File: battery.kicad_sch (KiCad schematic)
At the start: 41 parts, among them J1 Lipo, Q1 2N7002, Q2 IRLZ44N, Q3 AO3401A, Q4 IRLZ44N, SW1 SW_Push, SW2 SW_SPST, U1 BQ76920PW

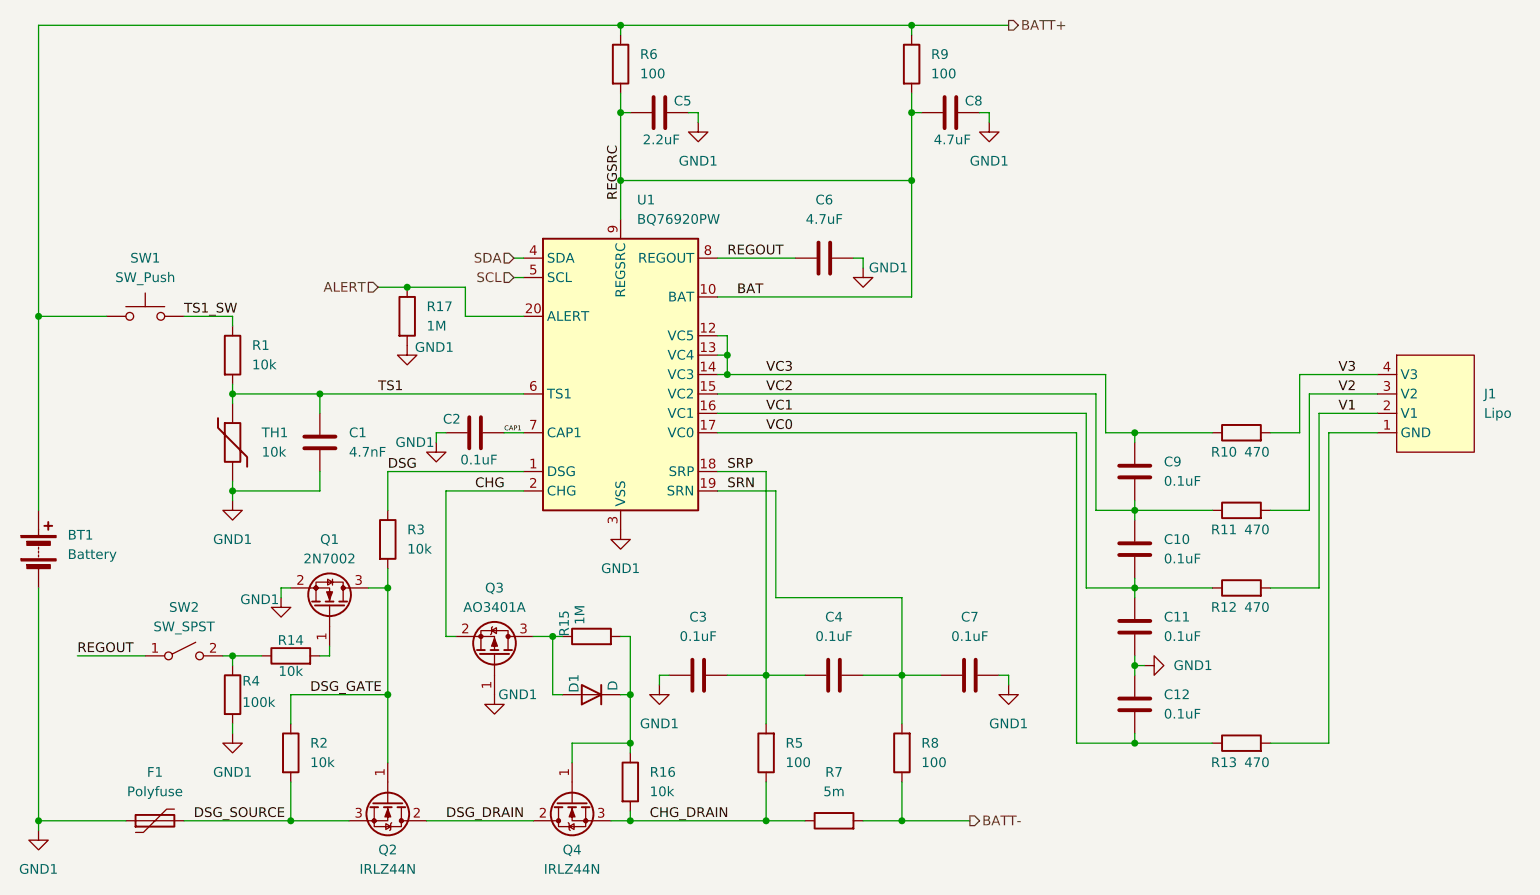
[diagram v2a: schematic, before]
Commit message: add frontleds
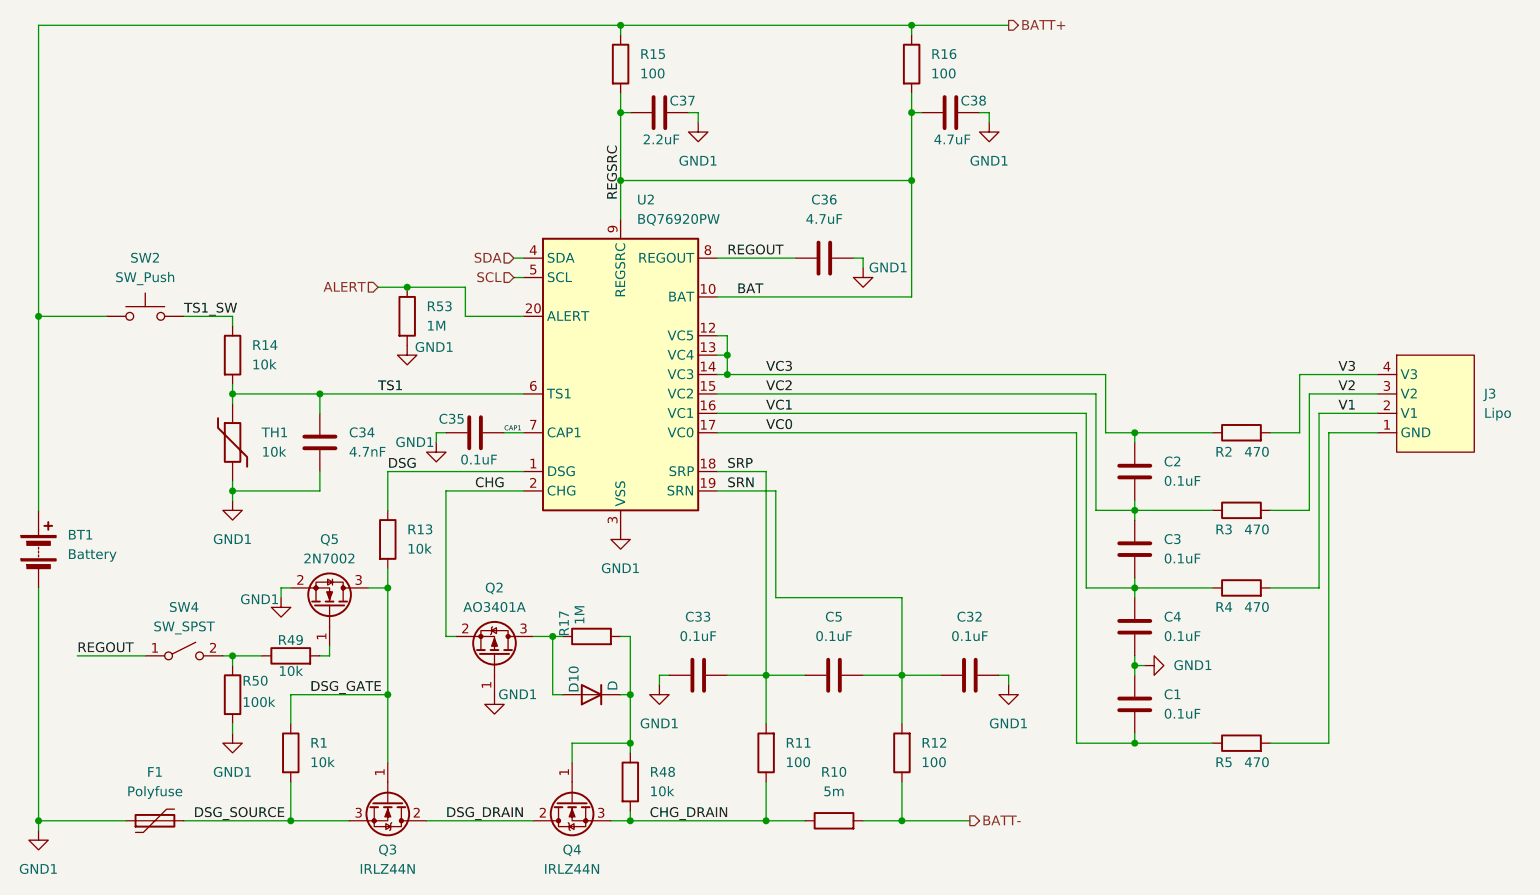
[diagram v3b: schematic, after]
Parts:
- renumbered C12 to C1, C9 to C2, C10 to C3, C7 to C32, C3 to C33, C1 to C34, C2 to C35, C6 to C36, C5 to C37, C8 to C38, C11 to C4, C4 to C5, D1 to D10, J1 to J3, Q3 to Q2, Q2 to Q3, Q1 to Q5, R2 to R1, R7 to R10, R5 to R11, R8 to R12, R3 to R13, R1 to R14, R6 to R15, R9 to R16, R15 to R17, R10 to R2, R11 to R3, R12 to R4, R16 to R48, R14 to R49, R13 to R5, R4 to R50, R17 to R53, SW1 to SW2, SW2 to SW4, U1 to U2
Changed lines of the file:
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@@
 		(dnp no)
 		(fields_autoplaced yes)
-		(property "Reference" "SW2"
+		(property "Reference" "SW4"
 			(at 109.22 115.57 0)
 			(effects
@@
 		(dnp no)
 		(fields_autoplaced yes)
-		(property "Reference" "R1"
+		(property "Reference" "R14"
 			(at 118.11 81.2799 0)
 			(effects
@@
 		(dnp no)
 		(fields_autoplaced yes)
-		(property "Reference" "R8"
+		(property "Reference" "R12"
 			(at 205.74 133.3499 0)
 			(effects
@@
 		(dnp no)
 		(fields_autoplaced yes)
-		(property "Reference" "C4"
+		(property "Reference" "C5"
 			(at 194.31 116.84 90)
 			(effects
@@
 		(on_board yes)
 		(dnp no)
-		(property "Reference" "#PWR013"
+		(property "Reference" "#PWR072"
 			(at 121.92 120.65 0)
 			(effects
@@
 		(on_board yes)
 		(dnp no)
-		(property "Reference" "R13"
+		(property "Reference" "R5"
 			(at 245.364 135.89 90)
 			(effects
@@
 		(on_board yes)
 		(dnp no)
-		(property "Reference" "D1"
+		(property "Reference" "D10"
 			(at 160.274 126.746 90)
 			(effects
@@
 		(on_board yes)
 		(dnp no)
-		(property "Reference" "Q3"
+		(property "Reference" "Q2"
 			(at 149.86 113.03 90)
 			(effects
@@
 		(dnp no)
 		(fields_autoplaced yes)
-		(property "Reference" "C1"
+		(property "Reference" "C34"
 			(at 130.81 92.7099 0)
 			(effects
@@
 		(dnp no)
 		(fields_autoplaced yes)
-		(property "Reference" "#PWR07"
+		(property "Reference" "#PWR034"
 			(at 176.53 58.42 0)
 			(effects
@@
 		(on_board yes)
 		(dnp no)
-		(property "Reference" "#PWR04"
+		(property "Reference" "#PWR028"
 			(at 149.86 133.35 0)
 			(effects
@@
 		(dnp no)
 		(fields_autoplaced yes)
-		(property "Reference" "R16"
+		(property "Reference" "R48"
 			(at 170.18 137.1599 0)
 			(effects
@@
 		(dnp no)
 		(fields_autoplaced yes)
-		(property "Reference" "C10"
+		(property "Reference" "C3"
 			(at 237.49 106.6799 0)
 			(effects
@@
 		(dnp no)
 		(fields_autoplaced yes)
-		(property "Reference" "#PWR05"
+		(property "Reference" "#PWR029"
 			(at 171.45 132.08 0)
 			(effects
@@
 		(dnp no)
 		(fields_autoplaced yes)
-		(property "Reference" "C3"
+		(property "Reference" "C33"
 			(at 176.53 116.84 90)
 			(effects
@@
 		(dnp no)
 		(fields_autoplaced yes)
-		(property "Reference" "#PWR02"
+		(property "Reference" "#PWR04"
 			(at 115.57 107.95 0)
 			(effects
@@
 		(dnp no)
 		(fields_autoplaced yes)
-		(property "Reference" "R6"
+		(property "Reference" "R15"
 			(at 168.91 43.1799 0)
 			(effects
@@
 		(dnp no)
 		(fields_autoplaced yes)
-		(property "Reference" "U1"
+		(property "Reference" "U2"
 			(at 168.5133 62.23 0)
 			(effects
@@
 		(dnp no)
 		(fields_autoplaced yes)
-		(property "Reference" "C6"
+		(property "Reference" "C36"
 			(at 193.04 62.23 90)
 			(effects
@@
 		(on_board yes)
 		(dnp no)
-		(property "Reference" "#PWR014"
+		(property "Reference" "#PWR0100"
 			(at 138.43 87.63 0)
 			(effects
@@
 		(dnp no)
 		(fields_autoplaced yes)
-		(property "Reference" "R7"
+		(property "Reference" "R10"
 			(at 194.31 137.16 90)
 			(effects
@@
 		(dnp no)
 		(fields_autoplaced yes)
-		(property "Reference" "#PWR012"
+		(property "Reference" "#PWR073"
 			(at 115.57 138.43 0)
 			(effects
@@
 		(dnp no)
 		(fields_autoplaced yes)
-		(property "Reference" "#PWR010"
+		(property "Reference" "#PWR033"
 			(at 214.63 58.42 0)
 			(effects
@@
 		(dnp no)
 		(fields_autoplaced yes)
-		(property "Reference" "Q2"
+		(property "Reference" "Q3"
 			(at 135.89 147.32 90)
 			(effects
@@
 		(dnp no)
 		(fields_autoplaced yes)
-		(property "Reference" "R2"
+		(property "Reference" "R1"
 			(at 125.73 133.3499 0)
 			(effects
@@
 		(on_board yes)
 		(dnp no)
-		(property "Reference" "Q1"
+		(property "Reference" "Q5"
 			(at 128.27 106.68 90)
 			(effects
@@
 		(dnp no)
 		(fields_autoplaced yes)
-		(property "Reference" "#PWR01"
+		(property "Reference" "#PWR03"
 			(at 90.17 151.13 0)
 			(effects
@@
 		(dnp no)
 		(fields_autoplaced yes)
-		(property "Reference" "R5"
+		(property "Reference" "R11"
 			(at 187.96 133.3499 0)
 			(effects
@@
 		(dnp no)
 		(fields_autoplaced yes)
-		(property "Reference" "#PWR011"
+		(property "Reference" "#PWR031"
 			(at 241.3 123.19 0)
 			(effects
@@
 		(dnp no)
 		(fields_autoplaced yes)
-		(property "Reference" "C9"
+		(property "Reference" "C2"
 			(at 237.49 96.5199 0)
 			(effects
@@
 		(dnp no)
 		(fields_autoplaced yes)
-		(property "Reference" "C12"
+		(property "Reference" "C1"
 			(at 237.49 126.9999 0)
 			(effects
@@
 		(on_board yes)
 		(dnp no)
-		(property "Reference" "R4"
+		(property "Reference" "R50"
 			(at 116.84 125.222 0)
 			(effects
@@
 		(on_board yes)
 		(dnp no)
-		(property "Reference" "#PWR03"
+		(property "Reference" "#PWR035"
 			(at 142.24 100.33 0)
 			(effects
@@
 		(on_board yes)
 		(dnp no)
-		(property "Reference" "R15"
+		(property "Reference" "R17"
 			(at 159.004 119.38 0)
 			(effects
@@
 		(on_board yes)
 		(dnp no)
-		(property "Reference" "#PWR08"
+		(property "Reference" "#PWR032"
 			(at 198.12 77.47 0)
 			(effects
@@
 		(dnp no)
 		(fields_autoplaced yes)
-		(property "Reference" "SW1"
+		(property "Reference" "SW2"
 			(at 104.14 69.85 0)
 			(effects
@@
 		(dnp no)
 		(fields_autoplaced yes)
-		(property "Reference" "J1"
+		(property "Reference" "J3"
 			(at 279.4 87.6299 0)
 			(effects
@@
 		(on_board yes)
 		(dnp no)
-		(property "Reference" "R10"
+		(property "Reference" "R2"
 			(at 245.364 95.25 90)
 			(effects
@@
 		(on_board yes)
 		(dnp no)
-		(property "Reference" "R12"
+		(property "Reference" "R4"
 			(at 245.364 115.57 90)
 			(effects
@@
 		(dnp no)
 		(fields_autoplaced yes)
-		(property "Reference" "R17"
+		(property "Reference" "R53"
 			(at 140.97 76.1999 0)
 			(effects
@@
 		(dnp no)
 		(fields_autoplaced yes)
-		(property "Reference" "C7"
+		(property "Reference" "C32"
 			(at 212.09 116.84 90)
 			(effects
@@
 		(dnp no)
 		(fields_autoplaced yes)
-		(property "Reference" "C11"
+		(property "Reference" "C4"
 			(at 237.49 116.8399 0)
 			(effects
@@
 		(on_board yes)
 		(dnp no)
-		(property "Reference" "C2"
+		(property "Reference" "C35"
 			(at 144.272 90.932 90)
 			(effects
@@
 		(on_board yes)
 		(dnp no)
-		(property "Reference" "C8"
+		(property "Reference" "C38"
 			(at 212.598 49.276 90)
 			(effects
@@
 		(on_board yes)
 		(dnp no)
-		(property "Reference" "R14"
+		(property "Reference" "R49"
 			(at 123.19 119.888 90)
 			(effects
@@
 		(on_board yes)
 		(dnp no)
-		(property "Reference" "C5"
+		(property "Reference" "C37"
 			(at 174.498 49.276 90)
 			(effects
@@
 		(on_board yes)
 		(dnp no)
-		(property "Reference" "R11"
+		(property "Reference" "R3"
 			(at 245.364 105.41 90)
 			(effects
@@
 		(dnp no)
 		(fields_autoplaced yes)
-		(property "Reference" "R3"
+		(property "Reference" "R13"
 			(at 138.43 105.4099 0)
 			(effects
@@
 		(dnp no)
 		(fields_autoplaced yes)
-		(property "Reference" "R9"
+		(property "Reference" "R16"
 			(at 207.01 43.1799 0)
 			(effects
@@
 		(dnp no)
 		(fields_autoplaced yes)
-		(property "Reference" "#PWR09"
+		(property "Reference" "#PWR030"
 			(at 217.17 132.08 0)
 			(effects
@@
 		(dnp no)
 		(fields_autoplaced yes)
-		(property "Reference" "#PWR06"
+		(property "Reference" "#PWR05"
 			(at 166.37 111.76 0)
 			(effects

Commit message: more stuff with switches n things
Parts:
- removed SW4: SW_SPST, Button_Switch_THT:SW_DIP_SPSTx01_Slide_9.78x4.72mm_W7.62mm_P2.54mm, symbol Switch:SW_SPST
- added J15: Conn_01x02_Pin, Connector:JWT_A3963_1x02_P3.96mm_Vertical, symbol Connector:Conn_01x02_Pin
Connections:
- net REGOUT: now also J15.2 (Pin_2)
- net at R49.1, R50.1: now also J15.1 (Pin_1)
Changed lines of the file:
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@@
 	(wire
 		(pts
-			(xy 114.3 121.92) (xy 115.57 121.92)
-		)
-		(stroke
-			(width 0)
-			(type default)
-		)
-	)
-	(wire
-		(pts
 			(xy 115.57 99.06) (xy 115.57 100.33)
 		)
@@
 	(wire
 		(pts
+			(xy 106.68 121.92) (xy 115.57 121.92)
+		)
+		(stroke
+			(width 0)
+			(type default)
+		)
+	)
+	(wire
+		(pts
 			(xy 186.69 114.3) (xy 186.69 100.33)
 		)
@@
 	)
 	(symbol
-		(lib_id "Switch:SW_SPST")
-		(at 109.22 121.92 0)
-		(unit 1)
-		(exclude_from_sim no)
-		(in_bom yes)
-		(on_board yes)
-		(dnp no)
-		(fields_autoplaced yes)
-		(property "Reference" "SW4"
-			(at 109.22 115.57 0)
-			(effects
-				(font
-					(size 1.27 1.27)
-				)
-			)
-		)
-		(property "Value" "SW_SPST"
-			(at 109.22 118.11 0)
-			(effects
-				(font
-					(size 1.27 1.27)
-				)
-			)
-		)
-		(property "Footprint" "Button_Switch_THT:SW_DIP_SPSTx01_Slide_9.78x4.72mm_W7.62mm_P2.54mm"
-			(at 109.22 121.92 0)
-			(effects
-				(font
-					(size 1.27 1.27)
-				)
-				(hide yes)
-			)
-		)
-		(property "Datasheet" "~"
-			(at 109.22 121.92 0)
-			(effects
-				(font
-					(size 1.27 1.27)
-				)
-				(hide yes)
-			)
-		)
-		(property "Description" "Single Pole Single Throw (SPST) switch"
-			(at 109.22 121.92 0)
-			(effects
-				(font
-					(size 1.27 1.27)
-				)
-				(hide yes)
-			)
-		)
-		(pin "1"
-		)
-		(pin "2"
-		)
-		(instances
-			(project ""
-				(path "/2f56b371-1597-47e1-a48d-b7f69d342f77/8e993949-53ac-4d46-9f7d-59c9cf3d33c4"
-					(reference "SW4")
-					(unit 1)
-				)
-			)
-			(project "battery"
-				(path "/5852dc9c-be81-4731-9c95-5e6ebdb17894"
-					(reference "SW2")
-					(unit 1)
-				)
-			)
-		)
-	)
-	(symbol
 		(lib_id "Device:R")
 		(at 115.57 82.55 0)
@@
 					(unit 1)
 				)
+			)
+		)
+	)
+	(symbol
+		(lib_id "Connector:Conn_01x02_Pin")
+		(at 106.68 116.84 270)
+		(unit 1)
+		(exclude_from_sim no)
+		(in_bom yes)
+		(on_board yes)
+		(dnp no)
+		(fields_autoplaced yes)
+		(property "Reference" "J15"
+			(at 107.95 116.2049 90)
+			(effects
+				(font
+					(size 1.27 1.27)
+				)
+				(justify left)
+			)
+		)
+		(property "Value" "Conn_01x02_Pin"
+			(at 107.95 118.7449 90)
+			(effects
+				(font
+					(size 1.27 1.27)
+				)
+				(justify left)
+			)
+		)
+		(property "Footprint" "Connector:JWT_A3963_1x02_P3.96mm_Vertical"
+			(at 106.68 116.84 0)
+			(effects
+				(font
+					(size 1.27 1.27)
+				)
+				(hide yes)
+			)
+		)
+		(property "Datasheet" "~"
+			(at 106.68 116.84 0)
+			(effects
+				(font
+					(size 1.27 1.27)
+				)
+				(hide yes)
+			)
+		)
+		(property "Description" "Generic connector, single row, 01x02, script generated"
+			(at 106.68 116.84 0)
+			(effects
+				(font
+					(size 1.27 1.27)
+				)
+				(hide yes)
+			)
+		)
+		(pin "1"
+		)
+		(pin "2"
+		)
+		(instances
+			(project ""
+				(path "/2f56b371-1597-47e1-a48d-b7f69d342f77/8e993949-53ac-4d46-9f7d-59c9cf3d33c4"
+					(reference "J15")
+					(unit 1)
+				)

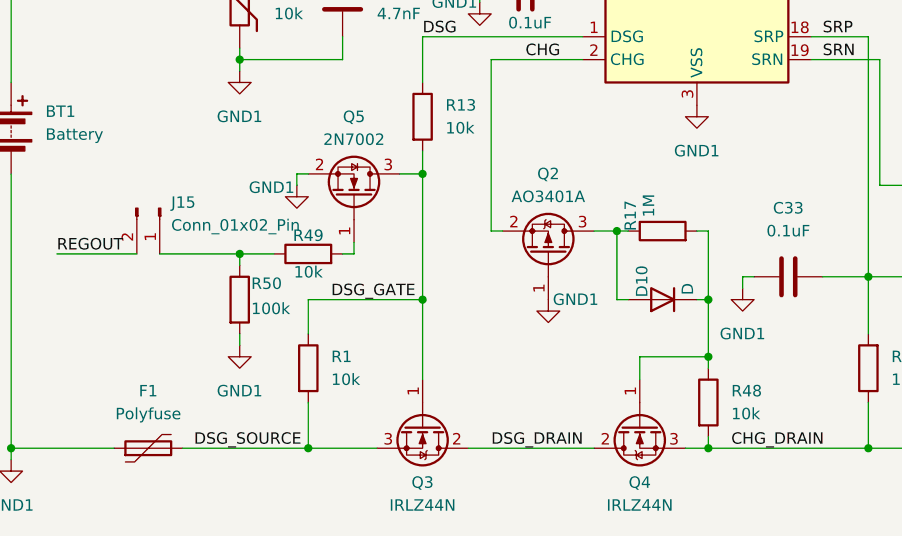
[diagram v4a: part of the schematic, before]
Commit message: added labels to everything
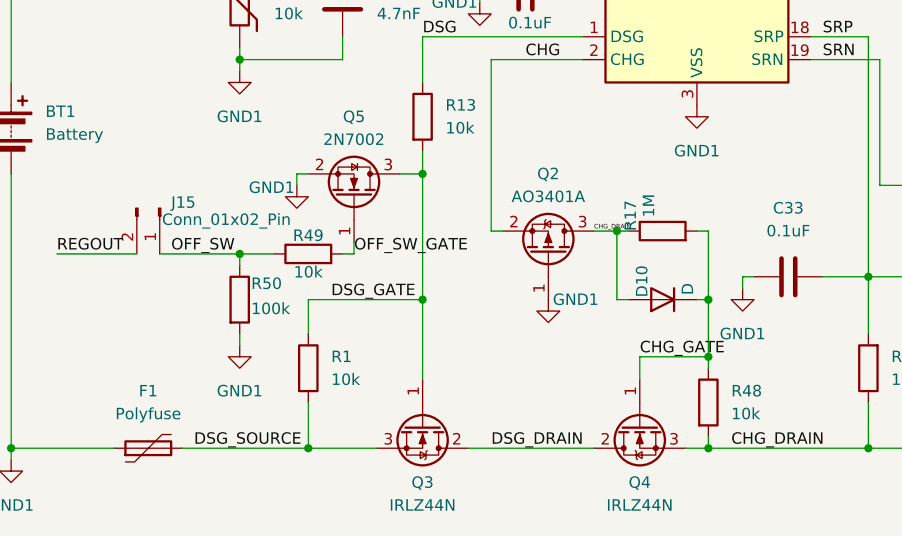
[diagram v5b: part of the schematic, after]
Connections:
- net CHG_DRAIN: now also D10.2 (A), Q2.3 (D), R17.1
- net CHG_GATE: now reaches D10.1 (K), Q4.1 (G), R17.2, R48.1
- net OFF_SW: now reaches J15.1 (Pin_1), R49.1, R50.1
- net OFF_SW_GATE: now reaches Q5.1 (G), R49.2
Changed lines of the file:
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@@
+		)
+	)
+	(label "OFF_SW"
+		(at 107.95 121.92 0)
+		(effects
+			(font
+				(size 1.27 1.27)
+			)
+			(justify left bottom)
 		)
 	)
@@
 		)
 	)
+	(label "CHG_DRAIN"
+		(at 154.94 119.38 0)
+		(effects
+			(font
+				(size 0.508 0.508)
+			)
+			(justify left bottom)
+		)
+	)
+	(label "CHG_GATE"
+		(at 160.02 133.35 0)
+		(effects
+			(font
+				(size 1.27 1.27)
+			)
+			(justify left bottom)
+		)
+	)
 	(label "CHG"
 		(at 147.32 100.33 0)
@@
 	(label "VC0"
 		(at 185.42 92.71 0)
+		(effects
+			(font
+				(size 1.27 1.27)
+			)
+			(justify left bottom)
+		)
+	)
+	(label "OFF_SW_GATE"
+		(at 128.27 121.92 0)
 		(effects
 			(font
@@
 		(on_board yes)
 		(dnp no)
-		(fields_autoplaced yes)
 		(property "Reference" "J15"
 			(at 107.95 116.2049 90)
@@
 		)
 		(property "Value" "Conn_01x02_Pin"
-			(at 107.95 118.7449 90)
-			(effects
-				(font
+			(at 106.934 118.11 90)
+			(effects
+				(font

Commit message: changes
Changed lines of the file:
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@@
-		)
-	)
-	(label "REGSRC"
-		(at 166.37 62.23 90)
-		(effects
-			(font
-				(size 1.27 1.27)
-			)
-			(justify left bottom)
 		)
 	)
@@
 					(unit 1)
 				)
+			)
+		)
+	)
+	(symbol
+		(lib_id "power:PWR_FLAG")
+		(at 166.37 50.8 90)
+		(unit 1)
+		(exclude_from_sim no)
+		(in_bom yes)
+		(on_board yes)
+		(dnp no)
+		(fields_autoplaced yes)
+		(property "Reference" "#FLG01"
+			(at 164.465 50.8 0)
+			(effects
+				(font
+					(size 1.27 1.27)
+				)
+				(hide yes)
+			)
+		)
+		(property "Value" "PWR_FLAG"
+			(at 162.56 50.7999 90)
+			(effects
+				(font
+					(size 1.27 1.27)
+				)
+				(justify left)
+			)
+		)
+		(property "Footprint" ""
+			(at 166.37 50.8 0)
+			(effects
+				(font
+					(size 1.27 1.27)
+				)
+				(hide yes)
+			)
+		)
+		(property "Datasheet" "~"
+			(at 166.37 50.8 0)
+			(effects
+				(font
+					(size 1.27 1.27)
+				)
+				(hide yes)
+			)
+		)
+		(property "Description" "Special symbol for telling ERC where power comes from"
+			(at 166.37 50.8 0)
+			(effects
+				(font
+					(size 1.27 1.27)
+				)
+				(hide yes)
+			)
+		)
+		(pin "1"
+		)
+		(instances
+			(project ""
+				(path "/2f56b371-1597-47e1-a48d-b7f69d342f77/8e993949-53ac-4d46-9f7d-59c9cf3d33c4"
+					(reference "#FLG01")
+					(unit 1)
+				)
